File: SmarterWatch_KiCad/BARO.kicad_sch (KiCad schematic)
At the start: 1 part

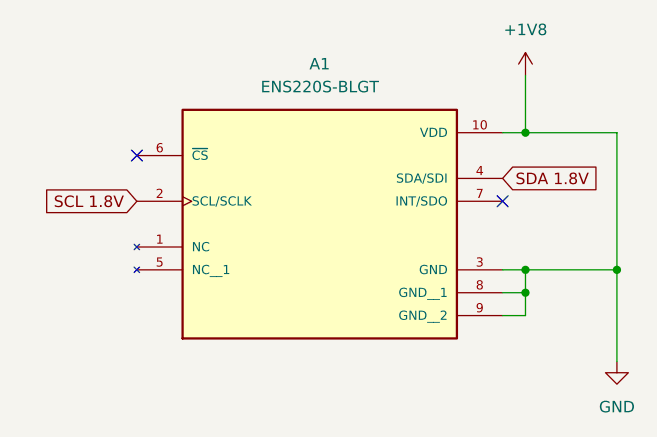
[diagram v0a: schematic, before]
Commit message: 1.8 to gnd
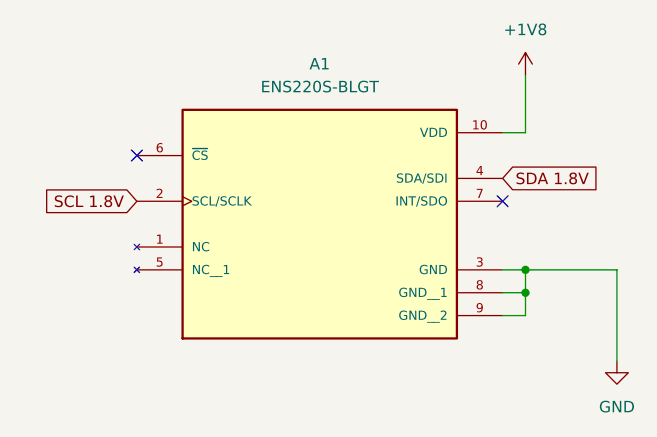
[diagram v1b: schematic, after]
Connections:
- net +1V8: no longer A1.3 (GND), A1.8 (GND__1), A1.9 (GND__2)
- new net GND: A1.3 (GND), A1.8 (GND__1), A1.9 (GND__2)
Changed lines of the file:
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@@
 	(paper "A4")
 	(junction
-		(at 171.45 115.57)
-		(diameter 0)
-		(color 0 0 0 0)
-	)
-	(junction
 		(at 161.29 115.57)
-		(diameter 0)
-		(color 0 0 0 0)
-	)
-	(junction
-		(at 161.29 100.33)
 		(diameter 0)
 		(color 0 0 0 0)
@@
 	(wire
 		(pts
-			(xy 161.29 100.33) (xy 171.45 100.33)
-		)
-		(stroke
-			(width 0)
-			(type default)
-		)
-	)
-	(wire
-		(pts
 			(xy 161.29 93.98) (xy 161.29 100.33)
 		)
 		(stroke
-			(width 0)
-			(type default)
-		)
-	)
-	(wire
-		(pts
-			(xy 171.45 115.57) (xy 171.45 100.33)
-		)
-		(stroke
